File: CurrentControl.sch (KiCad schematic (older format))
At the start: 7 parts, among them P1 CONN_01X01, Q401 BUK9575, U201 LMV358

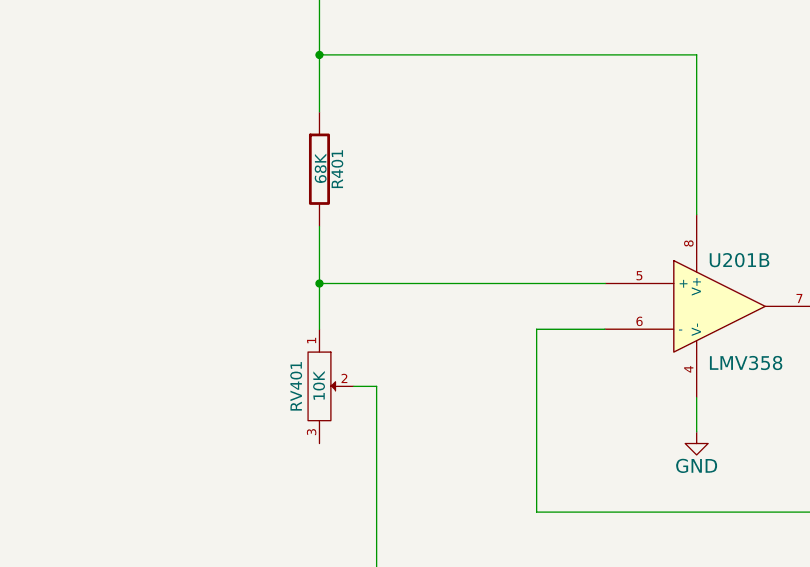
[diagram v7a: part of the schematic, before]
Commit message: added measure pins and ripup layout
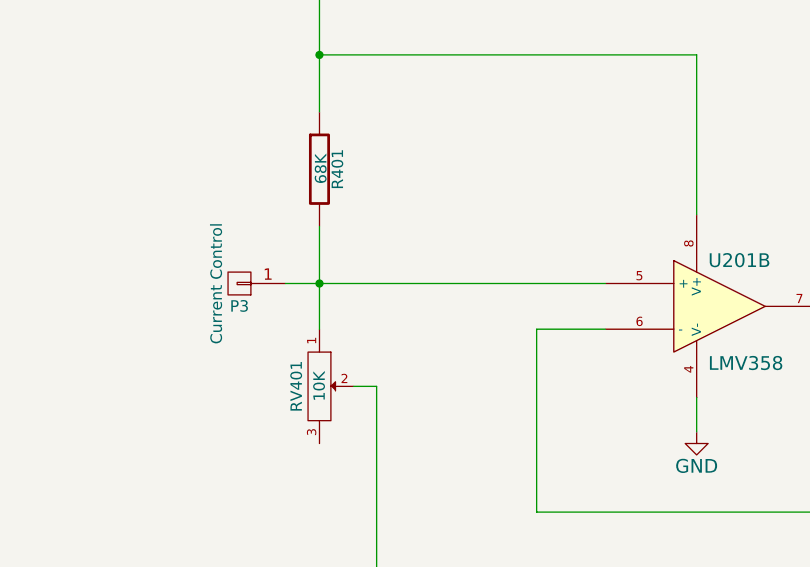
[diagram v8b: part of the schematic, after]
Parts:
- added P3: Current Control, symbol CONN_01X01
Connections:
- net at R401.2, RV401.1, U201.5 (+): now also P3.1 (P1)
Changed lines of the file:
@@
 $EndComp
 $Comp
-L GND #PWR06
+L GND #PWR7
 U 1 1 54DADC82
 P 5400 4250
-F 0 "#PWR06" H 5400 4000 60  0001 C CNN
+F 0 "#PWR7" H 5400 4000 60  0001 C CNN
 F 1 "GND" H 5400 4100 60  0000 C CNN
 F 2 "" H 5400 4250 60  0000 C CNN
@@
 Connection ~ 8100 4600
 Wire Wire Line
-	3750 3600 5000 3600
+	3600 3600 5000 3600
 Connection ~ 8100 5450
 $Comp
@@
 Wire Wire Line
 	4000 5450 8100 5450
+$Comp
+L CONN_01X01 P3
+U 1 1 54F1F408
+P 3400 3600
+F 0 "P3" H 3400 3700 50  0000 C CNN
+F 1 "Current Control" V 3500 3600 50  0000 C CNN
+F 2 "" H 3400 3600 60  0000 C CNN
+F 3 "" H 3400 3600 60  0000 C CNN
+	1    3400 3600
+	-1   0    0    1
+$EndComp
 $EndSCHEMATC
